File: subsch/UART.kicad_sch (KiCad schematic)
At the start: 2 parts, among them U2 CH340E

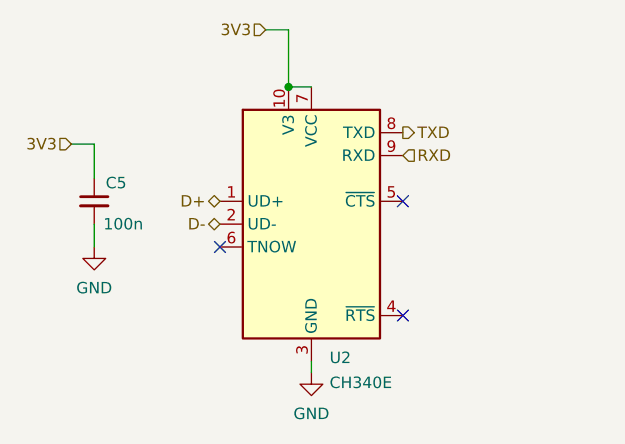
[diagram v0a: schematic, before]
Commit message: Change routings&Add ESD for UART and CAN&Add 5V protection and pull-resistance for GPIO
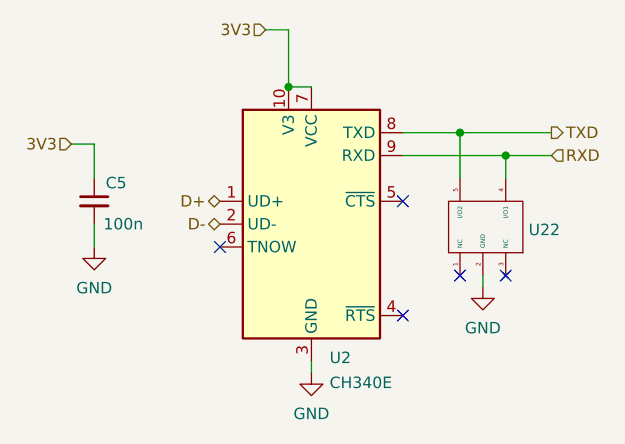
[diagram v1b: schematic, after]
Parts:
- added U22: ~, Package_TO_SOT_SMD:SOT-23-5, symbol Extra IC:ESDS314
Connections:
- net GND: now also U22.2 (GND)
- net RXD: now also U22.4 (I/O1)
- net TXD: now also U22.5 (I/O2)
- no-connect marks 3 -> 5
